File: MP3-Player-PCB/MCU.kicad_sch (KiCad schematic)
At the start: 24 parts, among them J101 Conn_ARM_SWD_TagConnect_TC2030, U101 STM32F411CEUx, Y101 8MHz

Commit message: Added 5.25k resistor to thermistor divider network as per BQ24259 datasheet
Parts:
- R101: JLCPCB Part # C25531 -> C25744
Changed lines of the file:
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@@
 			)
 		)
-		(property "JLCPCB Part #" "C25531"
+		(property "JLCPCB Part #" "C25744"
 			(at 129.54 66.04 90)
 			(effects

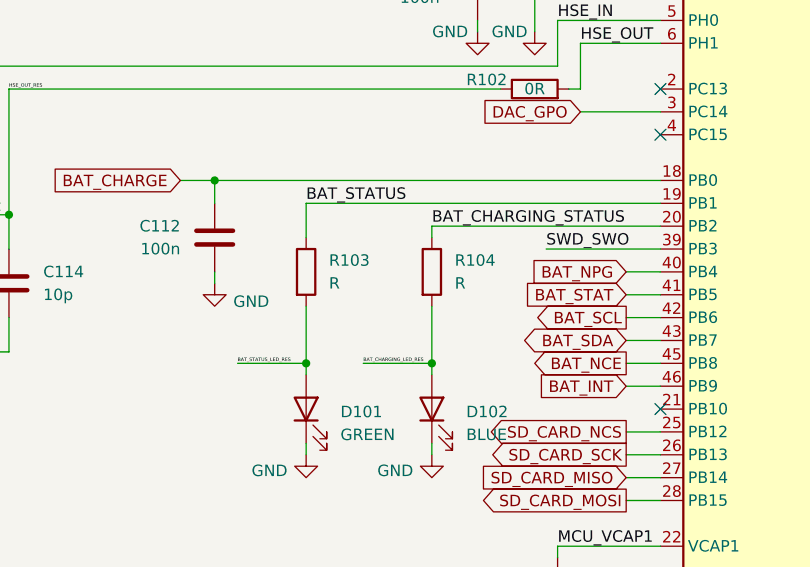
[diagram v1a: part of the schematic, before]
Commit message: Added JLCPCB part numbers for remaining parts
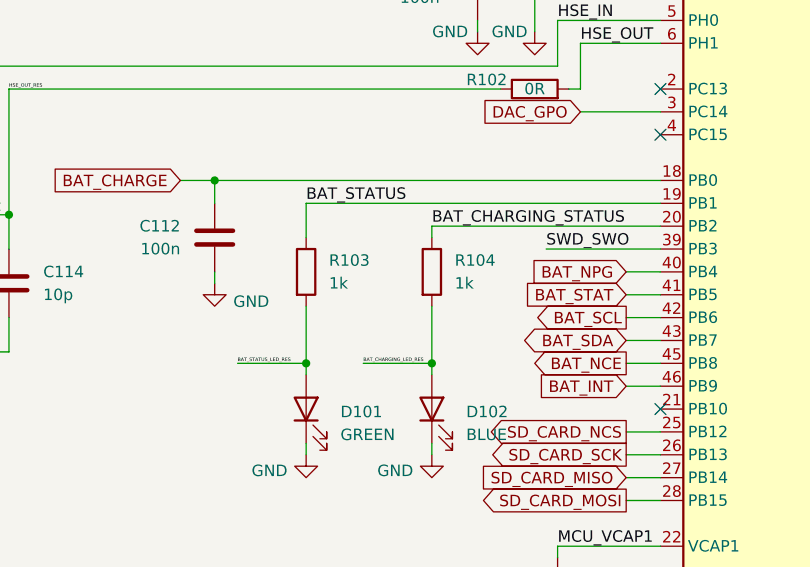
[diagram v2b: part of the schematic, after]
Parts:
- D101: JLCPCB Part # (none) -> C74338
- D102: JLCPCB Part # (none) -> C131223
- R103, R104: value R -> 1k; JLCPCB Part # (none) -> C11702
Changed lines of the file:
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@@
 			)
 		)
-		(property "Value" "R"
+		(property "Value" "1k"
 			(at 115.57 100.3299 0)
 			(effects
@@
 			)
 		)
-		(property "JLCPCB Part #" ""
+		(property "JLCPCB Part #" "C11702"
 			(at 113.03 99.06 0)
 			(effects
@@
 			)
 		)
-		(property "JLCPCB Part #" ""
+		(property "JLCPCB Part #" "C74338"
 			(at 99.06 114.3 90)
 			(effects
@@
 			)
 		)
-		(property "Value" "R"
+		(property "Value" "1k"
 			(at 101.6 100.3299 0)
 			(effects
@@
 			)
 		)
-		(property "JLCPCB Part #" ""
+		(property "JLCPCB Part #" "C11702"
 			(at 99.06 99.06 0)
 			(effects
@@
 			)
 		)
-		(property "JLCPCB Part #" ""
+		(property "JLCPCB Part #" "C131223"
 			(at 113.03 114.3 90)
 			(effects
